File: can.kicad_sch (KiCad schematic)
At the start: 27 parts, among them J1401 Conn_01x03, U1401 MCP2518FD-xQBB, U1402 TCAN1044A-Q1, U1403 ISO7721DR, X1401 40 MHz

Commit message: Weeded out all ERC errors
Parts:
- removed R1401: 330R, PCM_Resistor_SMD_AKL:R_0402_1005Metric, symbol Device:R
- C1401: renamed from C1402; LCSC (none) -> C1547
- C1402: renamed from C1403; LCSC (none) -> C1547
- C1403: renamed from C1401; value C_0402 -> 100nF; footprint PCM_Capacitor_SMD_AKL:C_0402_1005Metric -> Capacitor_SMD:C_0402_1005Metric; LCSC (none) -> C1525
- C1404: renamed from C1412; footprint PCM_Capacitor_SMD_AKL:C_0603_1608Metric -> Capacitor_SMD:C_0603_1608Metric
- C1405: renamed from C1413; footprint PCM_Capacitor_SMD_AKL:C_0402_1005Metric -> Capacitor_SMD:C_0402_1005Metric
- C1406: renamed from C1414; footprint PCM_Capacitor_SMD_AKL:C_0603_1608Metric -> Capacitor_SMD:C_0603_1608Metric
- C1408: renamed from C1416; footprint PCM_Capacitor_SMD_AKL:C_0603_1608Metric -> Capacitor_SMD:C_0603_1608Metric
- C1409: renamed from C1417; footprint PCM_Capacitor_SMD_AKL:C_0402_1005Metric -> Capacitor_SMD:C_0402_1005Metric
- C1410: renamed from C1418; footprint PCM_Capacitor_SMD_AKL:C_0603_1608Metric -> Capacitor_SMD:C_0603_1608Metric
- C1411: renamed from C1404; footprint PCM_Capacitor_SMD_AKL:C_0402_1005Metric -> Capacitor_SMD:C_0402_1005Metric
- C1412: renamed from C1407; footprint PCM_Capacitor_SMD_AKL:C_0603_1608Metric -> Capacitor_SMD:C_0603_1608Metric
- C1413: renamed from C1406; footprint PCM_Capacitor_SMD_AKL:C_0603_1608Metric -> Capacitor_SMD:C_0603_1608Metric
- D1401: footprint PCM_Package_TO_SOT_SMD_AKL:SOT-23 -> Package_TO_SOT_SMD:SOT-23
- J1401: footprint (none) -> Connector_PinHeader_2.54mm:PinHeader_1x03_P2.54mm_Vertical; LCSC (none) -> C49257
- JP1401: footprint SH-RPi:SolderJumper-2_P1.3mm_Open_TrianglePad_Narrow -> Connector_PinHeader_2.54mm:PinHeader_1x02_P2.54mm_Vertical; LCSC (none) -> C492401
- U1401: LCSC (none) -> C621395
- U1402: renamed from U1403; LCSC (none) -> C366164
- U1403: renamed from U1402; footprint (none) -> Package_SO:SOIC-8_3.9x4.9mm_P1.27mm; LCSC (none) -> C3234993
- renumbered C1415 to C1407, R1402 to R1401, R1403 to R1402
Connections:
- net +3V3 is gone; now on net CMx_3V3: C1403.2, U1401.14 (VDD)
- net CAN0_H is gone; now on net CANH_: R1401.2, R1402.2
- net CAN0_L is gone; now on net CANL_: JP1401.1 (A)
- net CANH: now reaches FL1401.1, J1401.2 (Pin_2)
- net CANL: now reaches FL1401.4, J1401.3 (Pin_3)
- net +3.3V renamed CMx_3V3
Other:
- note removed: "Dummy load to help with voltage regulation"
- company: Nabu Casa -> Hat Labs Oy
- title: Overview -> HALPI2

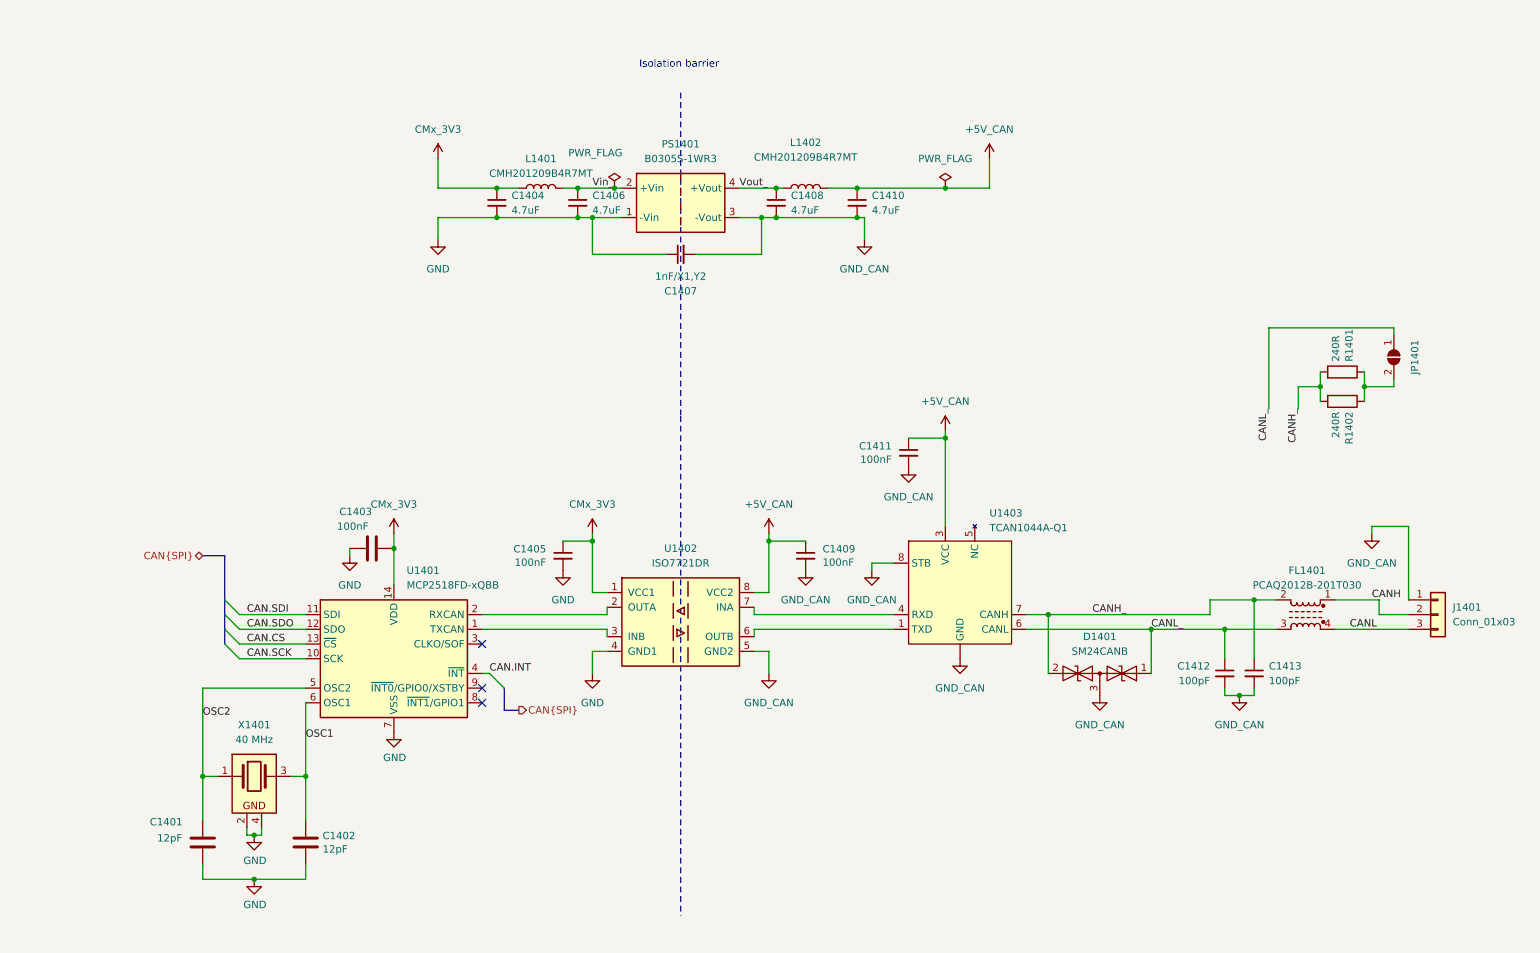
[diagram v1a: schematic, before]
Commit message: Implement ideal diodes for input and LDO power ORing
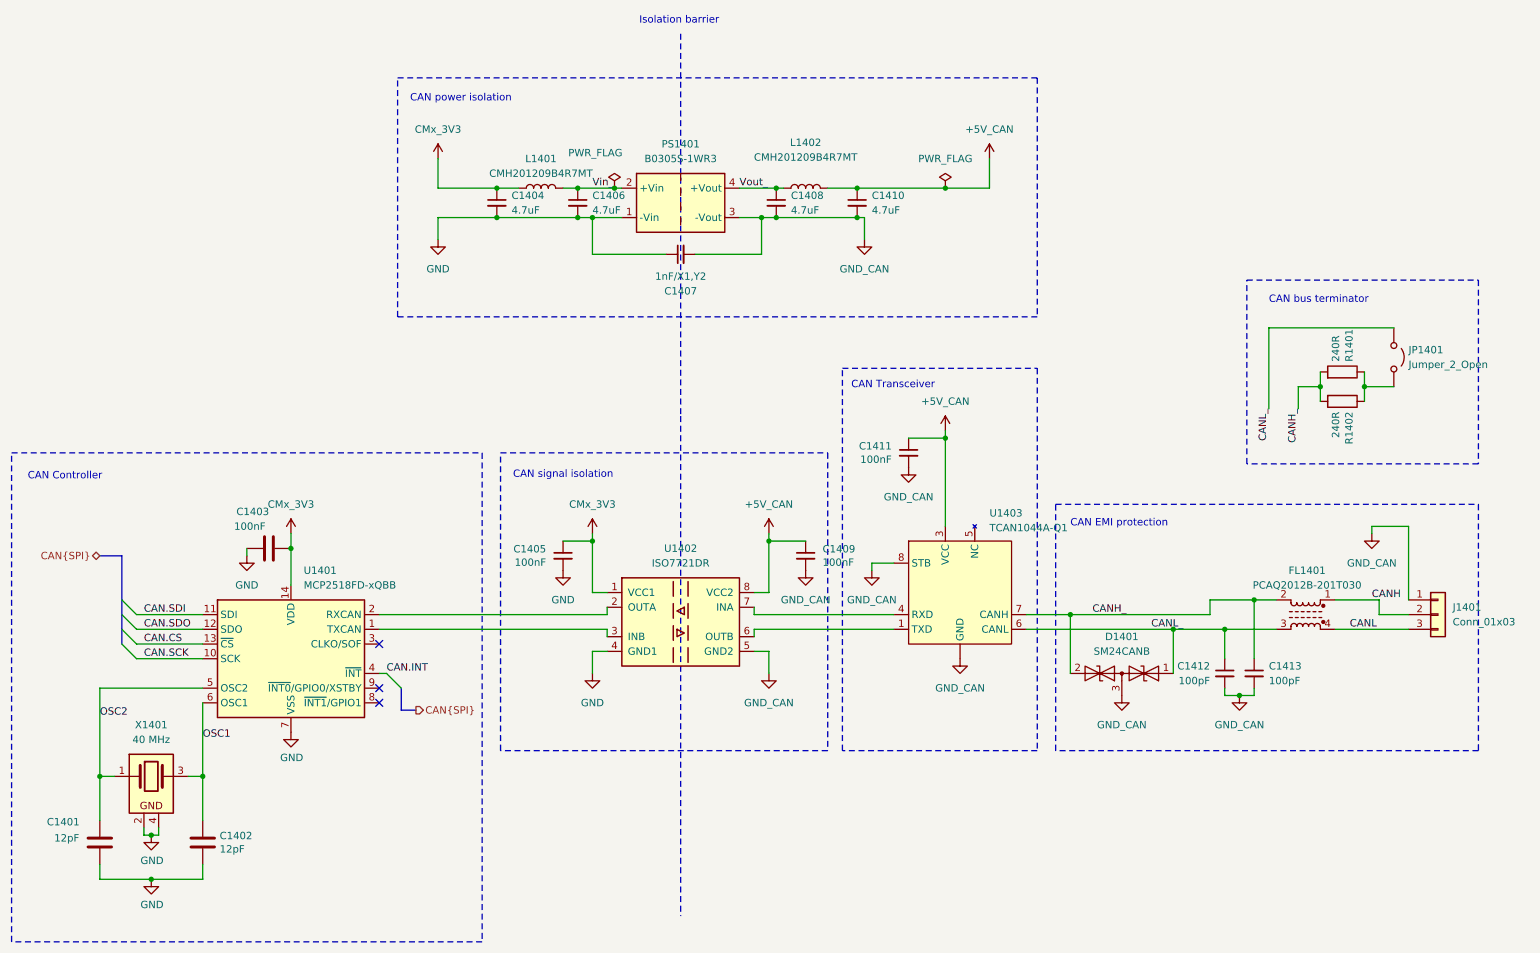
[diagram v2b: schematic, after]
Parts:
- removed JP1401: Term, Connector_PinHeader_2.54mm:PinHeader_1x02_P2.54mm_Vertical, symbol Jumper:SolderJumper_2_Open
- added JP1401: Jumper_2_Open, Connector_PinHeader_2.54mm:PinHeader_1x02_P2.54mm_Vertical, symbol Jumper:Jumper_2_Open
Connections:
- net CANL_: now also JP1401.1 (A)
- net at R1401.1, R1402.1: now also JP1401.2 (B)
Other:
- note added: "CAN Controller"
- note added: "CAN EMI protection"
- note added: "CAN Transceiver"
- note added: "CAN bus terminator"
- note added: "CAN power isolation"
- note added: "CAN signal isolation"
- moved on the sheet: C1401, C1402, C1403, D1401, U1401, X1401

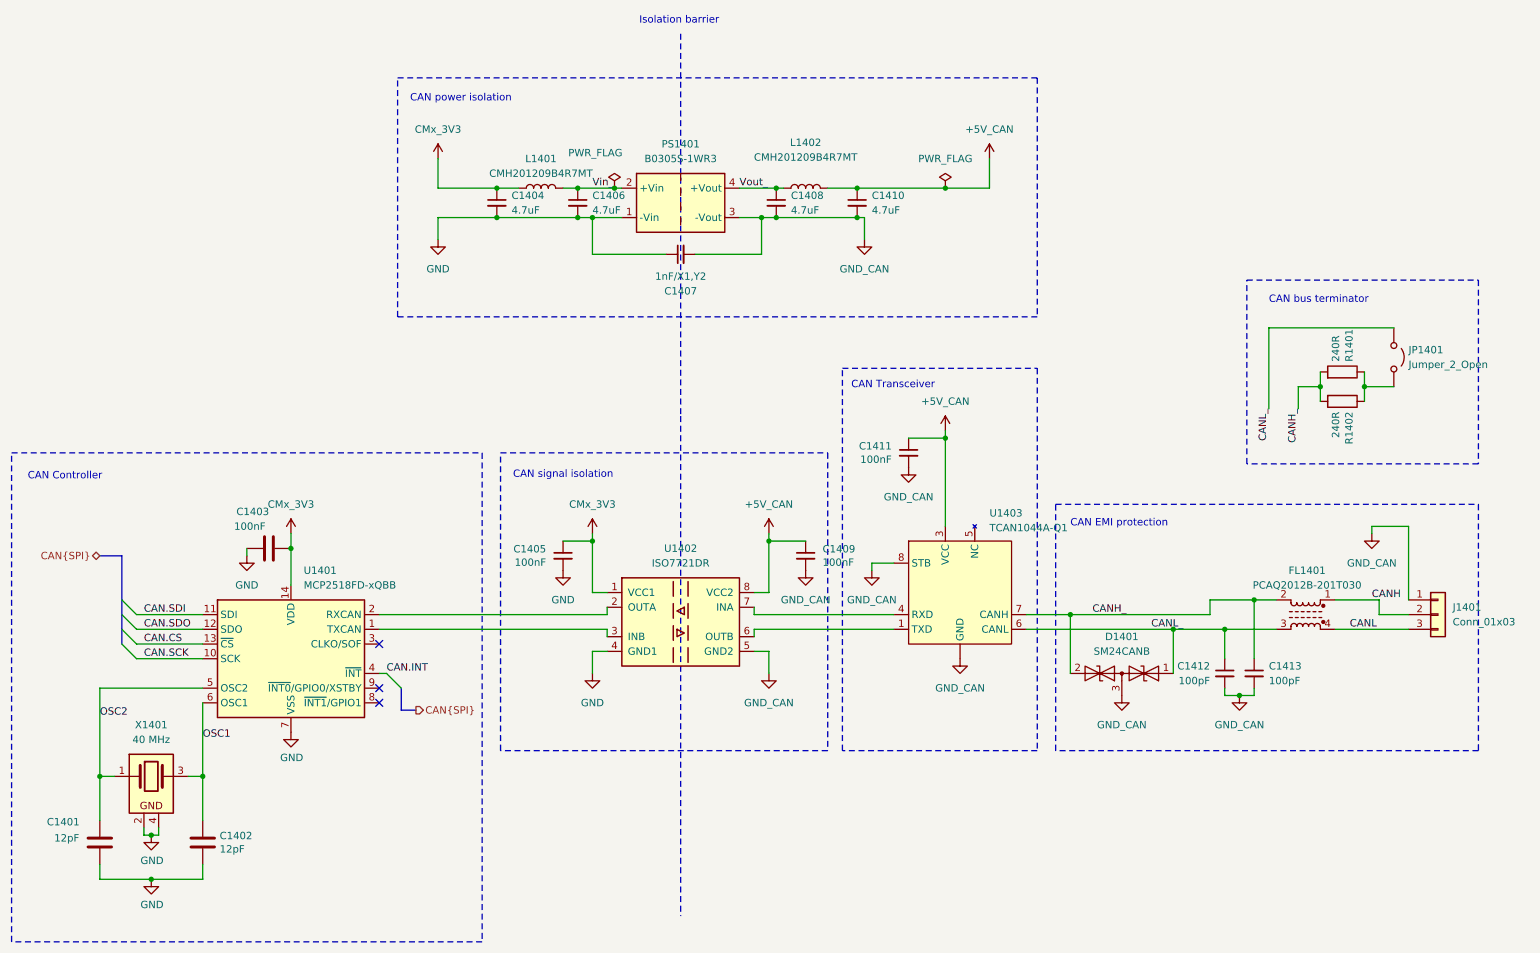
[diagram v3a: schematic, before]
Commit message: Sprinkle test points on the schematics
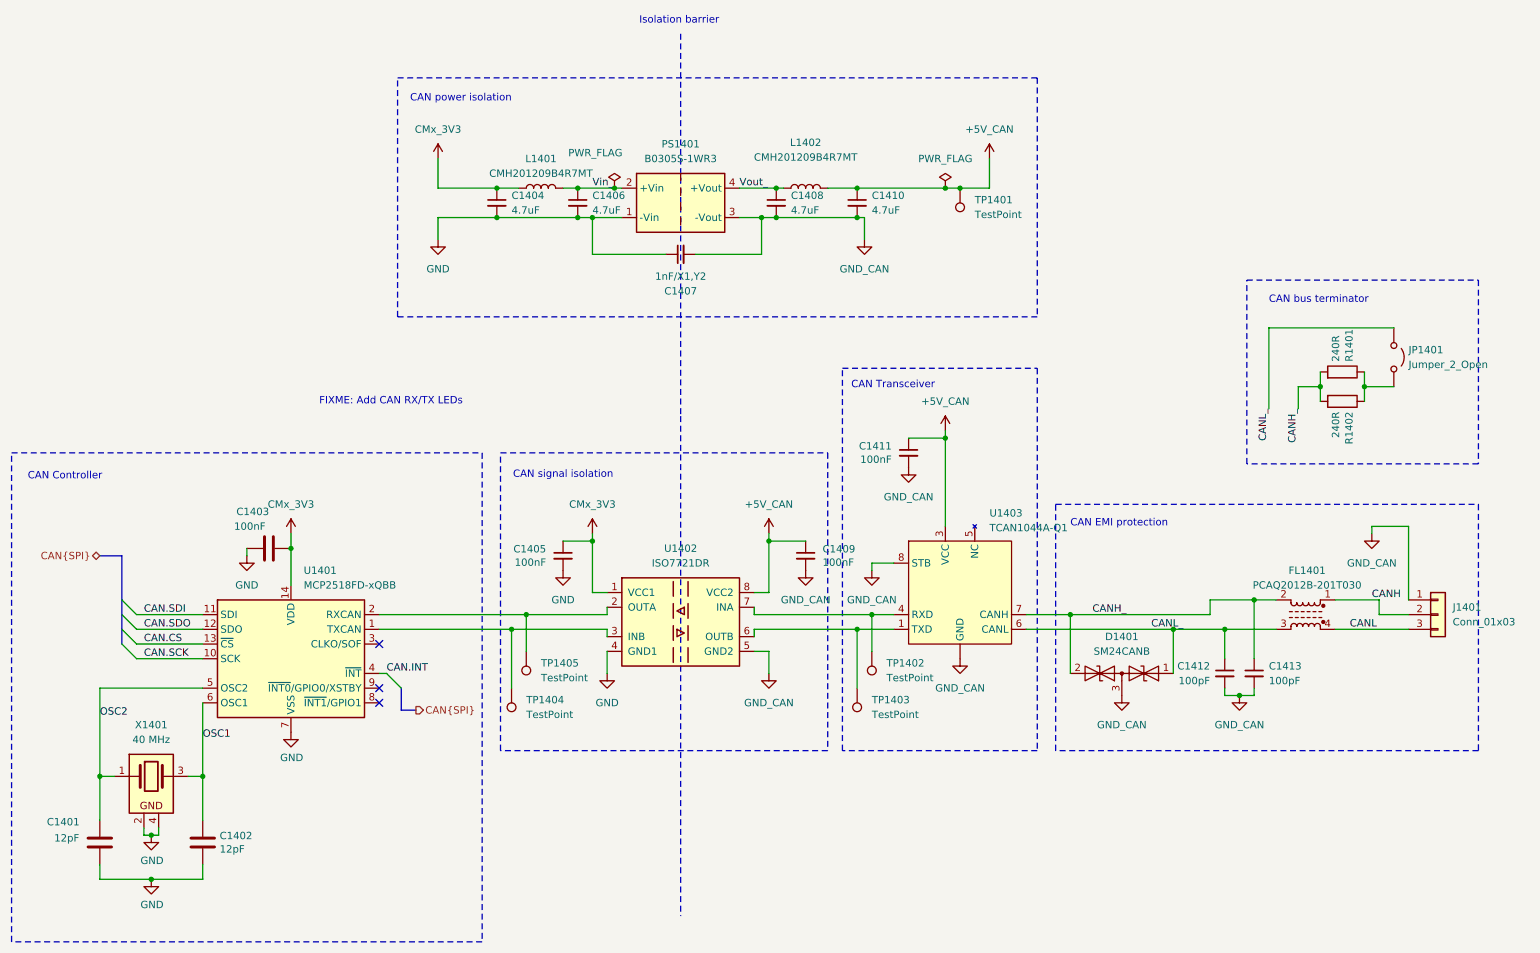
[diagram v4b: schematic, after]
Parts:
- added TP1401, TP1402, TP1403, TP1404, TP1405: TestPoint, TestPoint:TestPoint_Pad_D1.0mm, symbol Connector:TestPoint
- C1407: footprint HALSER:C_1808_4520Metric -> Hatlabs:C_1808_4520Metric
- FL1401: footprint HALSER:L_CommonModeChoke_PCAQ2012B -> Hatlabs:L_CommonModeChoke_PCAQ2012B
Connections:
- net +5V_CAN: now also TP1401.1
- net at U1401.1 (TXCAN), U1402.3 (INB): now also TP1404.1
- net at U1401.2 (RXCAN), U1402.2 (OUTA): now also TP1405.1
- net at U1402.6 (OUTB), U1403.1 (TXD): now also TP1403.1
- net at U1402.7 (INA), U1403.4 (RXD): now also TP1402.1
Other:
- note added: "FIXME: Add CAN RX/TX LEDs"

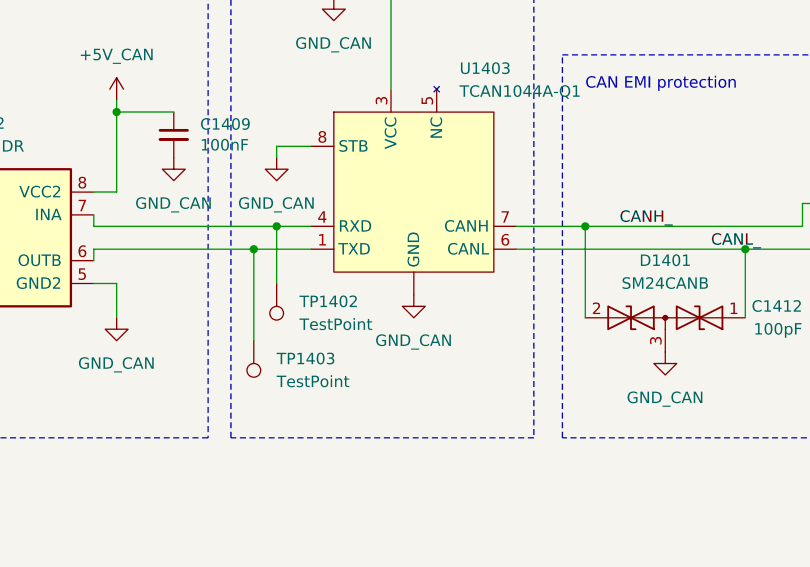
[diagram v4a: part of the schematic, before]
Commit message: Fix ethernet port & other changes
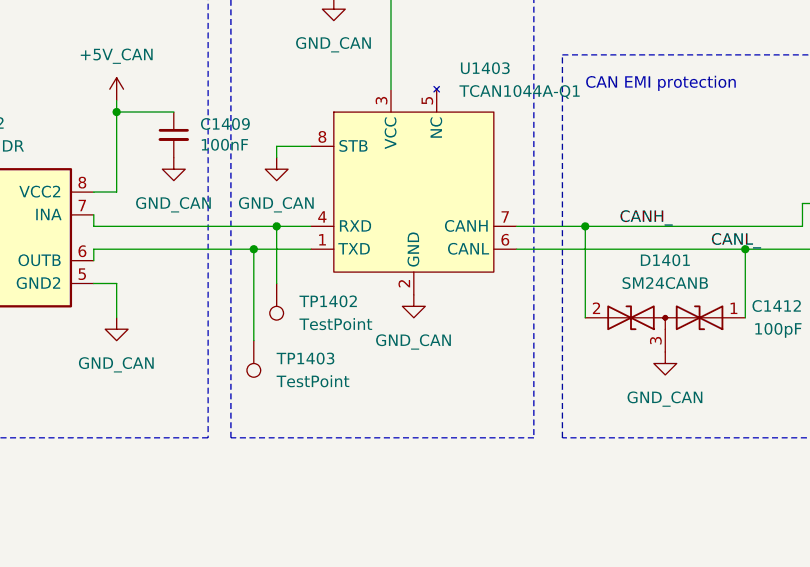
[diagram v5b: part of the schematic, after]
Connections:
- net GND_CAN: now also U1403.2 (GND); no longer U1403. (GND)
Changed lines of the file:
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@@
 		(pin "8"
 		)
-		(pin ""
+		(pin "2"
 		)
 		(pin "5"

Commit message: Implement a USB3 hub
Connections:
- net CMx_3V3 renamed +3.3VCMx
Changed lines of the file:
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@@
 			)
 		)
+		(property "Sim.Enable" ""
+			(at 184.15 49.53 0)
+			(effects
+				(font
+					(size 1.27 1.27)
+				)
+				(hide yes)
+			)
+		)
 		(pin "1"
 		)
@@
 	)
 	(symbol
-		(lib_id "power:+3V3")
+		(lib_id "Hatlabs:+3.3VCMx")
 		(at 120.65 109.22 0)
 		(unit 1)
@@
 			)
 		)
-		(property "Value" "CMx_3V3"
-			(at 120.65 104.14 0)
+		(property "Value" "+3.3VCMx"
+			(at 123.19 107.9499 0)
 			(effects
 				(font
 					(size 1.27 1.27)
 				)
+				(justify left)
 			)
 		)
@@
 			)
 		)
-		(property "Description" "Power symbol creates a global label with name \"+3V3\""
+		(property "Description" "Power symbol driven by the CMx module +3.3V output"
 			(at 120.65 109.22 0)
 			(effects
@@
 			)
 		)
+		(property "Sim.Enable" ""
+			(at 168.91 129.54 0)
+			(effects
+				(font
+					(size 1.27 1.27)
+				)
+				(hide yes)
+			)
+		)
 		(pin "1"
 		)
@@
 	)
 	(symbol
-		(lib_id "power:+3V3")
+		(lib_id "Hatlabs:+3.3VCMx")
 		(at 68.58 109.22 0)
 		(unit 1)
@@
 			)
 		)
-		(property "Value" "CMx_3V3"
-			(at 68.58 104.14 0)
+		(property "Value" "+3.3VCMx"
+			(at 71.12 107.9499 0)
 			(effects
 				(font
 					(size 1.27 1.27)
 				)
+				(justify left)
 			)
 		)
@@
 			)
 		)
-		(property "Description" "Power symbol creates a global label with name \"+3V3\""
+		(property "Description" "Power symbol driven by the CMx module +3.3V output"
 			(at 68.58 109.22 0)
 			(effects
@@
 		(at 259.08 78.74 270)
 		(unit 1)
-		(exclude_from_sim yes)
+		(exclude_from_sim no)
 		(in_bom yes)
 		(on_board yes)
@@
 			)
 		)
+		(property "Sim.Enable" ""
+			(at 166.37 135.89 0)
+			(effects
+				(font
+					(size 1.27 1.27)
+				)
+				(hide yes)
+			)
+		)
 		(pin "1"
 		)
@@
 			)
 		)
+		(property "Sim.Enable" ""
+			(at 106.68 135.89 0)
+			(effects
+				(font
+					(size 1.27 1.27)
+				)
+				(hide yes)
+			)
+		)
 		(pin "1"
 		)
@@
 	)
 	(symbol
-		(lib_id "power:+3V3")
+		(lib_id "Hatlabs:+3.3VCMx")
 		(at 93.98 44.45 0)
 		(unit 1)
@@
 			)
 		)
-		(property "Value" "CMx_3V3"
-			(at 93.98 39.37 0)
+		(property "Value" "+3.3VCMx"
+			(at 96.52 43.1799 0)
 			(effects
 				(font
 					(size 1.27 1.27)
 				)
+				(justify left)
 			)
 		)
@@
 			)
 		)
-		(property "Description" "Power symbol creates a global label with name \"+3V3\""
+		(property "Description" "Power symbol driven by the CMx module +3.3V output"
 			(at 93.98 44.45 0)
 			(effects
@@
 			(at 109.22 129.54 0)
 			(effects
+				(font
+					(size 1.27 1.27)
+				)
+				(hide yes)
+			)
+		)
+		(property "Sim.Enable" ""
+			(at 109.22 129.54 0)
+			(effects

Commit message: Finish component selection for USB3 hub
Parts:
- JP1401: LCSC (none) -> C492401
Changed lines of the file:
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@@
+			)
+		)
+		(property "LCSC" "C492401"
+			(at 259.08 78.74 0)
+			(effects
+				(font
+					(size 1.27 1.27)
+				)
+				(hide yes)
 			)
 		)
